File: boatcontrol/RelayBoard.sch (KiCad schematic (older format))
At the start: 15 parts, among them J2301 Conn_02x20_Odd_Even Header, J2302 TBL008V-1000-08BE, J2303 TBL008V-1000-08BE, K2301 EW60-1A3-CL12D04, K2302 EW60-1A3-CL12D04, K2303 EW60-1A3-CL12D04, K2304 EW60-1A3-CL12D04, K2305 EW60-1A3-CL12D04, K2306 EW60-1A3-CL12D04, K2307 EW60-1A3-CL12D04, K2308 EW60-1A3-CL12D04

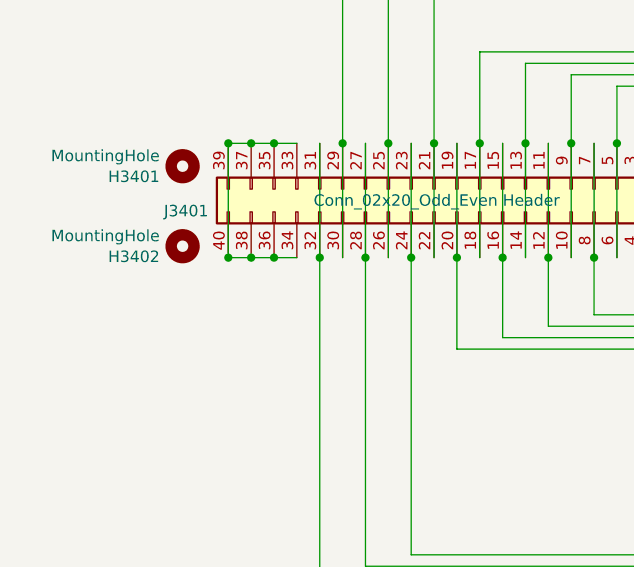
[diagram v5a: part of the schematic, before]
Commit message: Route missing track
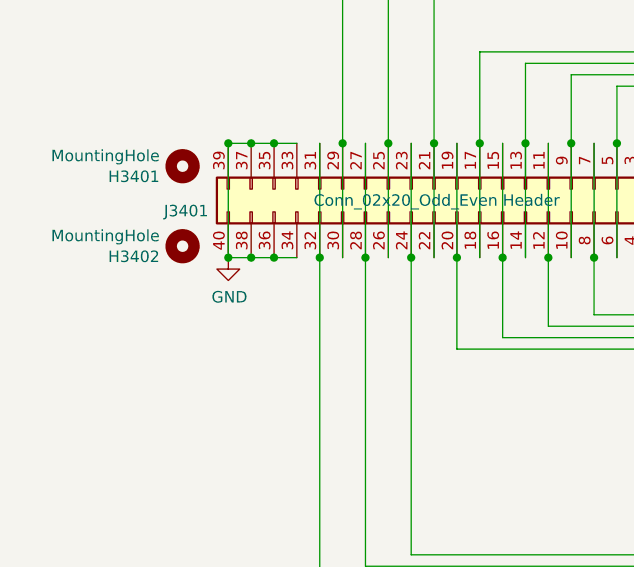
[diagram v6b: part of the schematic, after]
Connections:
- net GND: now also J2301.33 (Pin_33), J2301.34 (Pin_34), J2301.35 (Pin_35), J2301.36 (Pin_36), J2301.37 (Pin_37), J2301.38 (Pin_38), J2301.39 (Pin_39), J2301.40 (Pin_40)
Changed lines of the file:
@@
 Connection ~ 250  3800
 Connection ~ 250  4300
+$Comp
+L power:GND #PWR?
+U 1 1 60E5FB29
+P 250 4300
+F 0 "#PWR?" H 250 4050 50  0001 C CNN
+F 1 "GND" H 255 4127 50  0000 C CNN
+F 2 "" H 250 4300 50  0001 C CNN
+F 3 "" H 250 4300 50  0001 C CNN
+	1    250  4300
+	1    0    0    -1
+$EndComp
 $EndSCHEMATC
